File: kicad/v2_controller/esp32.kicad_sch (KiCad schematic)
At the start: 21 parts, among them J3 Conn_02x10_Odd_Even, J4 Conn_02x10_Odd_Even, J5 Conn_02x04_Odd_Even, J6 Conn_02x03_Odd_Even, Q1 S8050, Q2 S8050, SW18 Boot, SW19 Reset, U3 74AHCT1G125

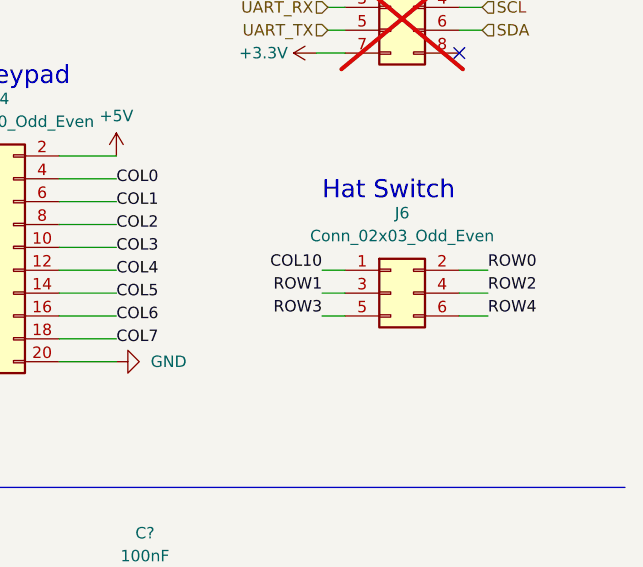
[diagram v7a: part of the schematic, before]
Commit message: [kicad] a little more trace routing
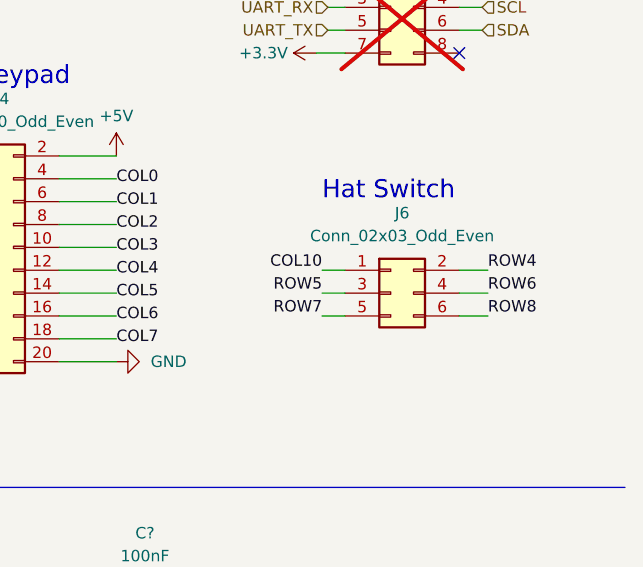
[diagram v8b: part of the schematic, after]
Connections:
- net ROW0: no longer J6.2 (Pin_2)
- net ROW1: no longer J6.3 (Pin_3)
- net ROW2: no longer J6.4 (Pin_4)
- net ROW3: no longer J6.5 (Pin_5)
- net ROW4: now also J6.2 (Pin_2); no longer J6.6 (Pin_6)
- net ROW5: now also J6.3 (Pin_3)
- net ROW6: now also J6.4 (Pin_4)
- net ROW7: now also J6.5 (Pin_5)
- net ROW8: now also J6.6 (Pin_6)
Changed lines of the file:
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@@
     (effects (font (size 3 3) (thickness 1) bold (color 194 0 0 1)) (justify left bottom))
   )
-  (label "ROW3" (at 251.46 101.6 180) (fields_autoplaced)
+  (label "ROW7" (at 251.46 101.6 180) (fields_autoplaced)
     (effects (font (size 1.27 1.27)) (justify right bottom))
   )
@@
     )
   )
-  (label "ROW0" (at 269.875 96.52 0) (fields_autoplaced)
+  (label "ROW4" (at 269.875 96.52 0) (fields_autoplaced)
     (effects (font (size 1.27 1.27)) (justify left bottom))
   )
@@
     )
   )
-  (label "ROW2" (at 269.875 99.06 0) (fields_autoplaced)
+  (label "ROW6" (at 269.875 99.06 0) (fields_autoplaced)
     (effects (font (size 1.27 1.27)) (justify left bottom))
   )
@@
     )
   )
-  (label "ROW1" (at 251.46 99.06 180) (fields_autoplaced)
-    (effects (font (size 1.27 1.27)) (justify right bottom))
-  )
-  (label "ROW4" (at 269.875 101.6 0) (fields_autoplaced)
-    (effects (font (size 1.27 1.27)) (justify left bottom))
-  )
+  (label "ROW5" (at 251.46 99.06 180) (fields_autoplaced)
+    (effects (font (size 1.27 1.27)) (justify right bottom))
+  )
+  (label "ROW8" (at 269.875 101.6 0) (fields_autoplaced)
+    (effects (font (size 1.27 1.27)) (justify left bottom))
+  )
